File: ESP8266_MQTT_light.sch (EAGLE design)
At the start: 29 parts, among them IC2 7805DT, J1 DCJ0202, J2 RGBW1, Q1 IRF3704S, Q2 IRF3704S, Q3 IRF3704S, Q4 IRF3704S, SW1 2-1825910-7, SW2 2-1825910-7, SW3 2-1825910-7

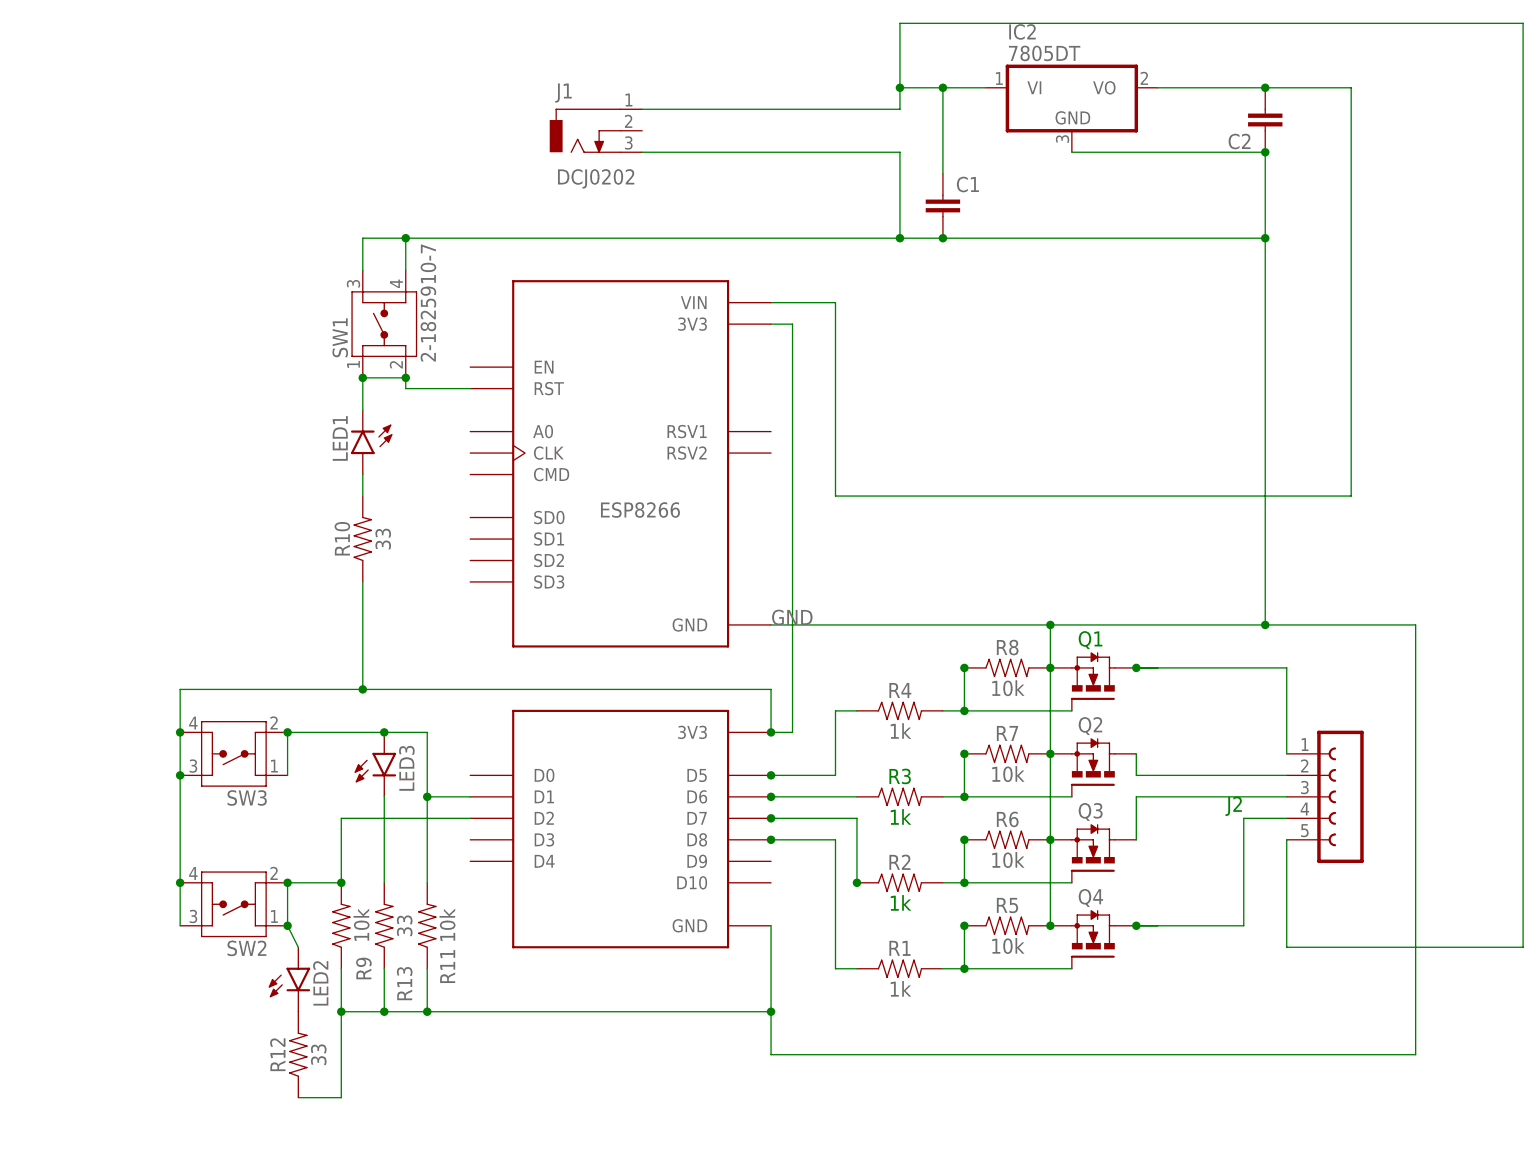
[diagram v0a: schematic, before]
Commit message: Changed Switch on board
The original board had an error on the switch
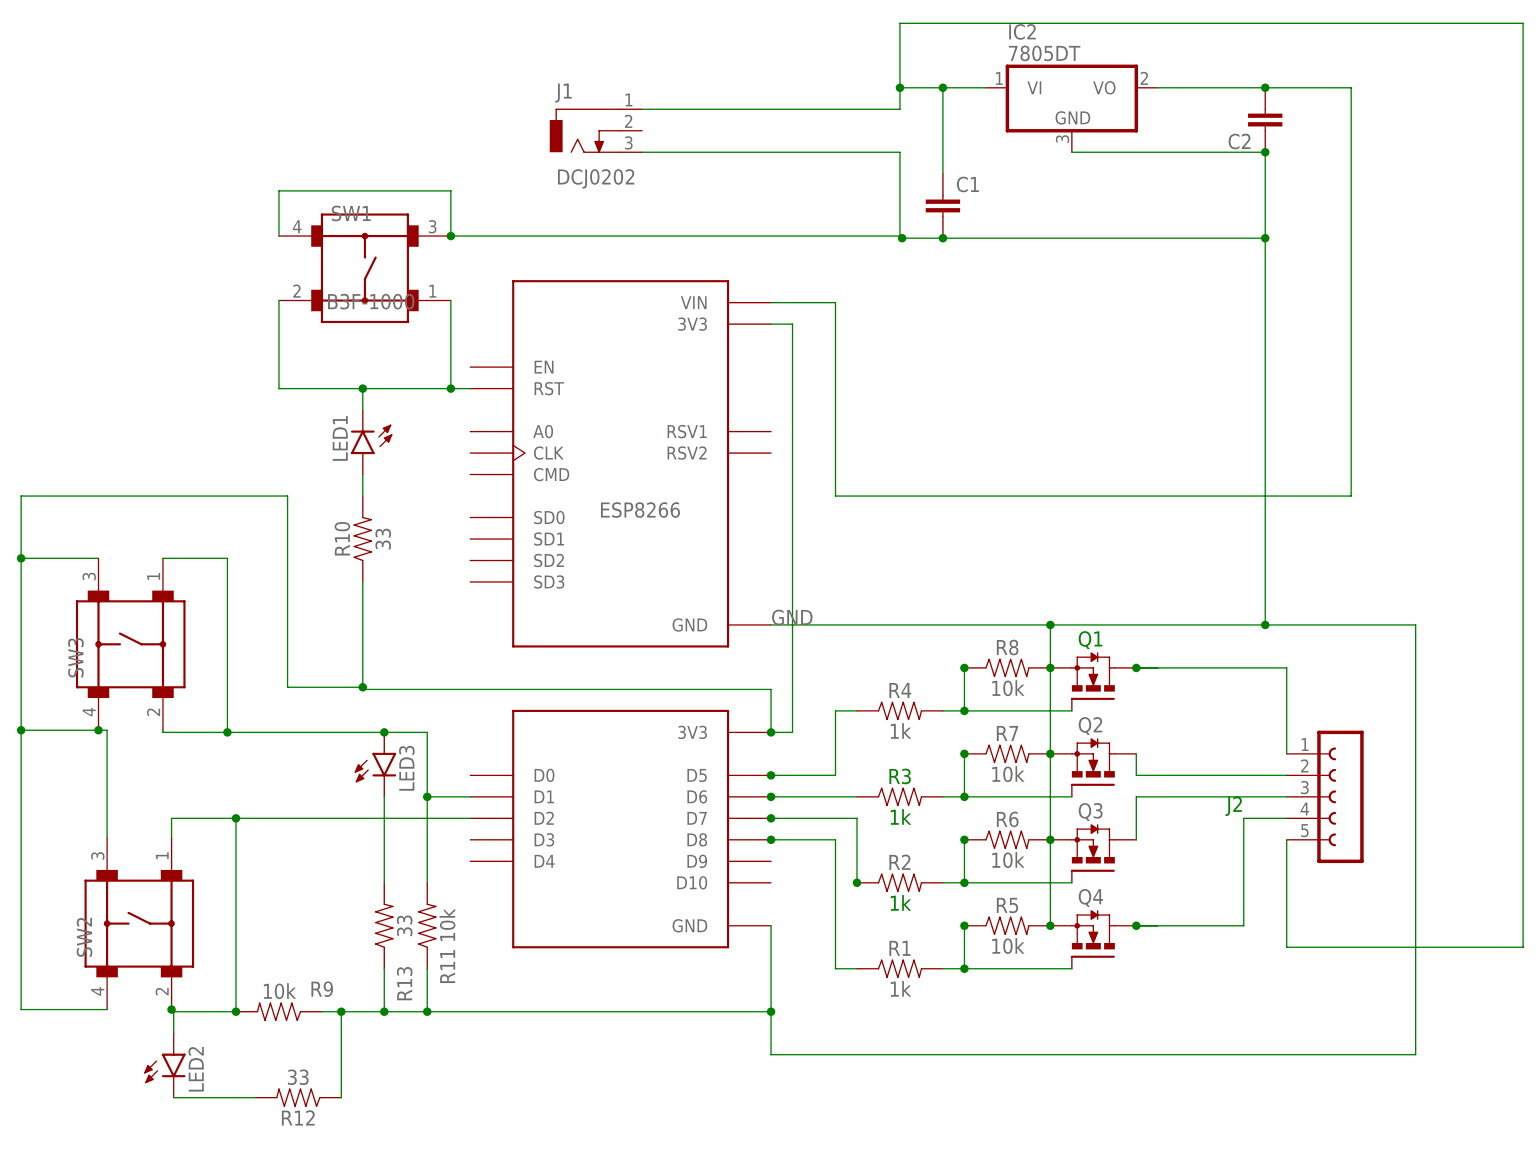
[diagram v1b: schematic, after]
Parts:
- SW1, SW2, SW3: value 2-1825910-7 -> B3F-1000; device Switch:2-1825910-7 -> Switch:B3F-1000
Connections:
- net M-CTL renamed N$5
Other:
- moved on the sheet: LED2, R12, R9

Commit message: Changed Resistor footprint
I changed the resistors to a 1206 SMD footprint
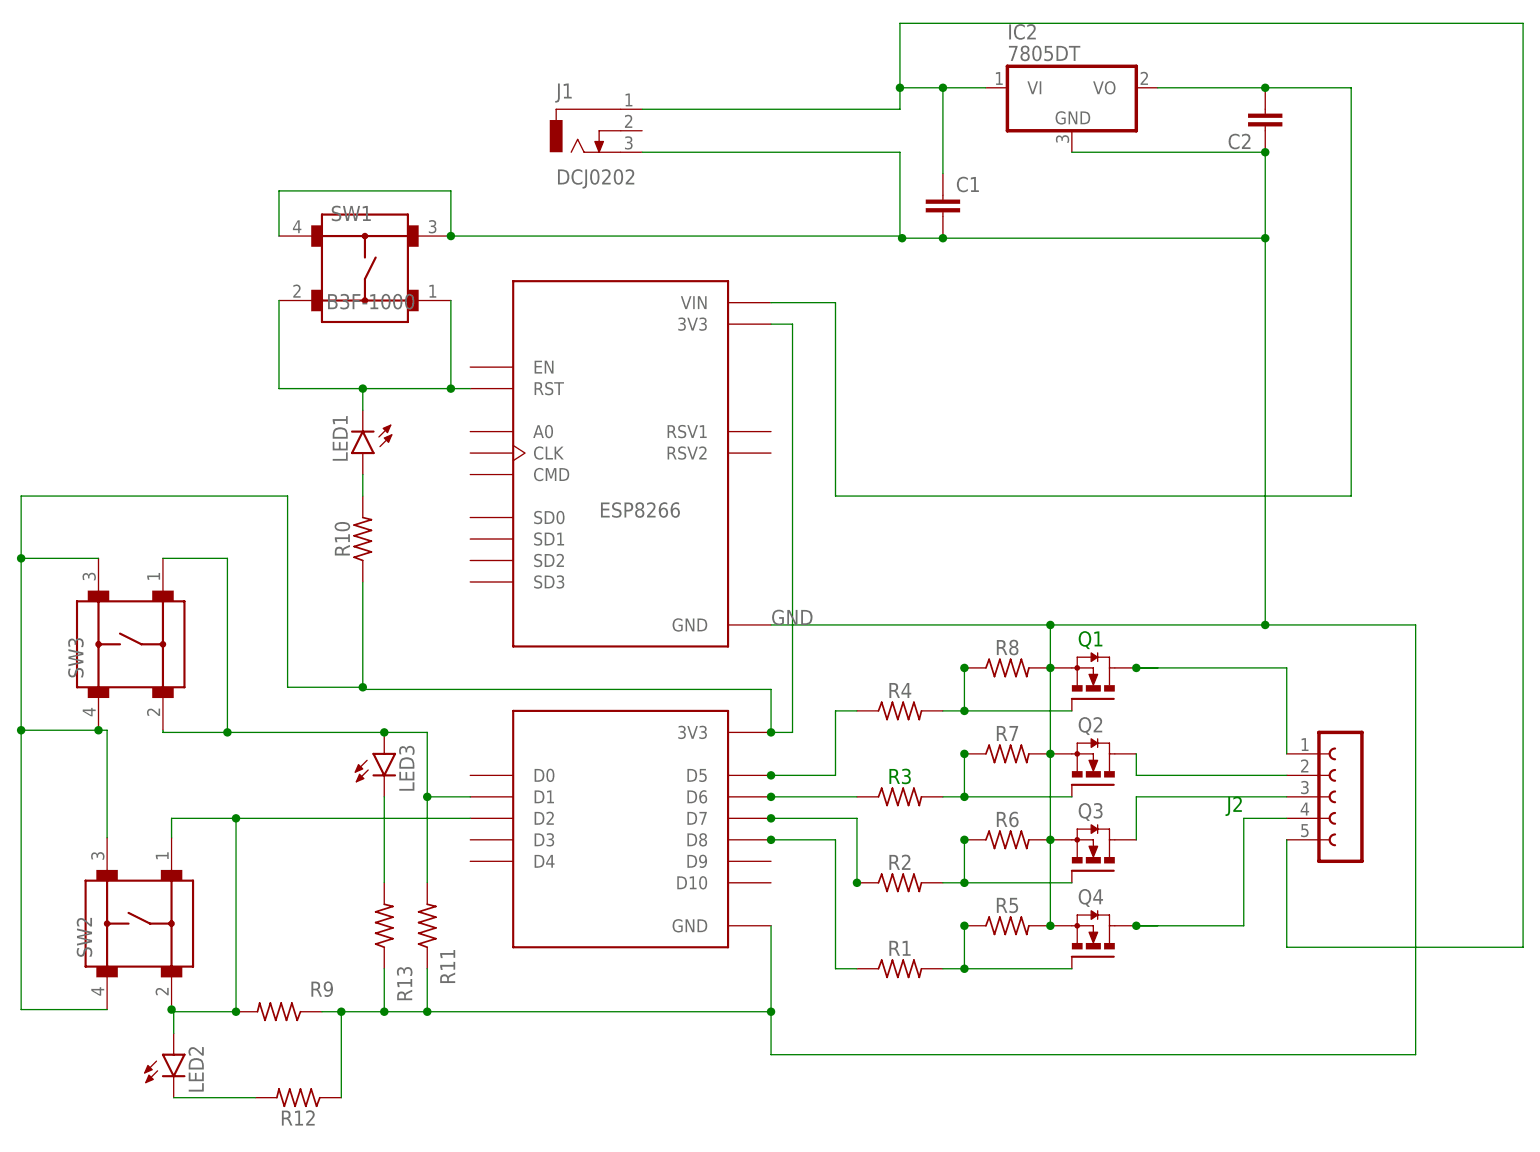
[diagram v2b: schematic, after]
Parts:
- R1, R2, R3, R4: device SparkFun-Resistors:1KOHM-0603-1/10W-1% -> rcl:R-US_R1206
- R10, R12, R13: device SparkFun-Resistors:33OHM-0603-1/10W-1% -> rcl:R-US_R1206
- R11, R5, R6, R7, R8, R9: device SparkFun-Resistors:10KOHM-0603-1/10W-1% -> rcl:R-US_R1206
